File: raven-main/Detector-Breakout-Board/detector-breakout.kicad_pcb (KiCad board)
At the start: 2 copper layers, 46 parts, among them J1 DeployLipo, J3 Conn_01x04, J9 UCLipo, Q1 SQJQ100EL, U7 TPS7A4701xRGW

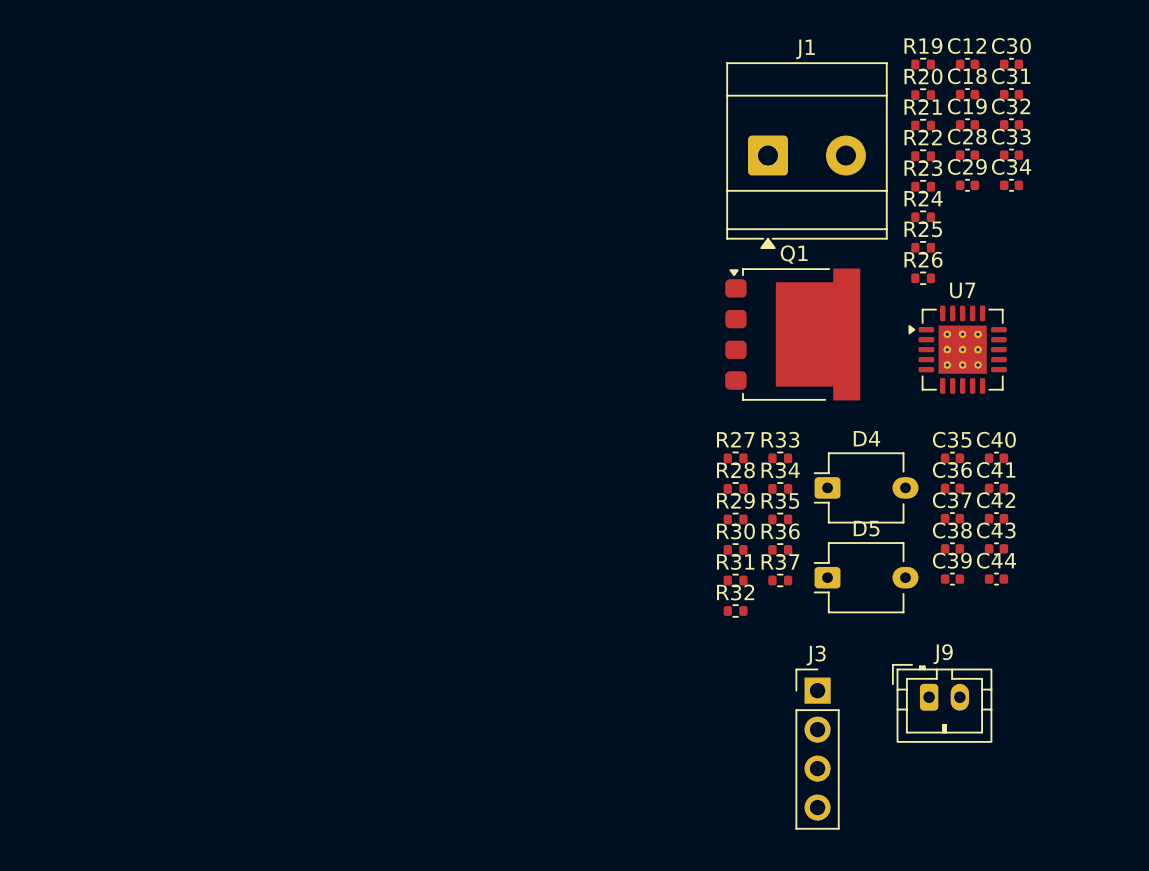
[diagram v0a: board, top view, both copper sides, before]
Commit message: Updated pcb layout
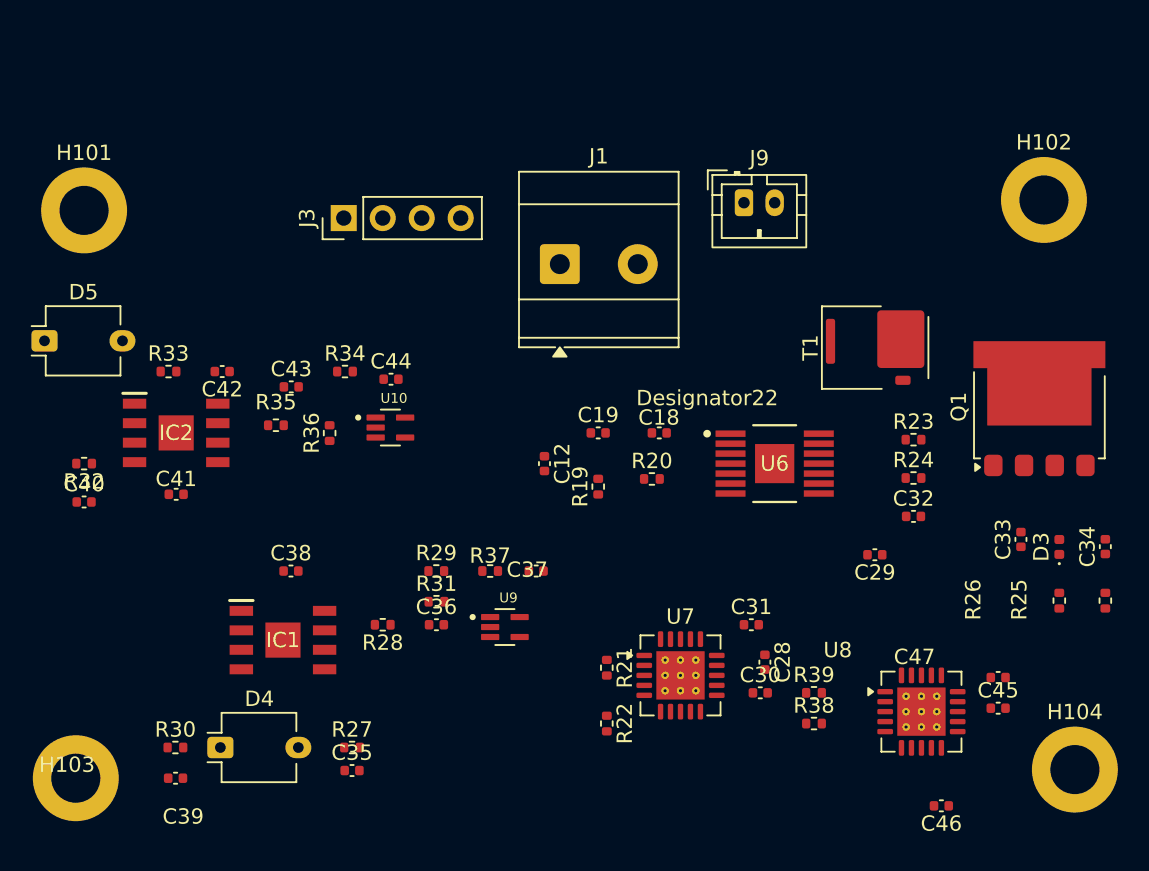
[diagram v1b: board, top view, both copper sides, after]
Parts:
- added C45: 10uF, Capacitor_SMD:C_0402_1005Metric, F.Cu at (133.1, 90.4)
- added C46: 1uF, Capacitor_SMD:C_0402_1005Metric, F.Cu at (129.4, 96.8)
- added C47: 47uF, Capacitor_SMD:C_0402_1005Metric, F.Cu at (133.1, 88.4)
- added D3: D, Diode_SMD:D_0402_1005Metric, F.Cu at (137.0, 79.9)
- added H101: MountingHole_Pad, MountingHole:MountingHole_3.2mm_M3_DIN965_Pad, F.Cu at (73.5, 58.0)
- added H102: MountingHole_Pad, MountingHole:MountingHole_3.2mm_M3_DIN965_Pad, F.Cu at (136.0, 57.3)
- added H103: MountingHole_Pad, MountingHole:MountingHole_3.2mm_M3_DIN965_Pad, F.Cu at (73.0, 95.0)
- added H104: MountingHole_Pad, MountingHole:MountingHole_3.2mm_M3_DIN965_Pad, F.Cu at (138.1, 94.4)
- added IC1: ADA4817-1ARDZ-R7, ADA4817-1ARDZ-R7:SOIC127P600X175-9N, F.Cu at (86.5, 86.0)
- added IC2: ADA4817-1ARDZ-R7, ADA4817-1ARDZ-R7:SOIC127P600X175-9N, F.Cu at (79.5, 72.5)
- added R38: 13.3k, Resistor_SMD:R_0402_1005Metric, F.Cu at (121.1, 91.4)
- added R39: 9.76k, Resistor_SMD:R_0402_1005Metric, F.Cu at (121.1, 89.4)
- added T1: Transformer_1P_1S, Transistor_Power:GaN_Systems_GaNPX-3_5x6.6mm_Drain2.93x0.6mm, F.Cu at (125.0, 66.9)
- added U10: TLV3201AIDCKT, TLV3201AIDCKT:SOT65P210X110-5N, F.Cu at (93.5, 72.2)
- added U6: LM5185QPWPRQ1, footprints:PWP0014G-IPC_A, F.Cu at (118.5, 74.5)
- added U8: TPS7A4701xRGW, Package_DFN_QFN:Texas_RGW0020A_VQFN-20-1EP_5x5mm_P0.65mm_EP3.15x3.15mm_ThermalVias, F.Cu at (128.1, 90.7)
- added U9: TLV3201AIDCKT, TLV3201AIDCKT:SOT65P210X110-5N, F.Cu at (100.9, 85.2)
- R22: value 10k -> 9.76k
- moved C40 59.5 mm to (73.5, 77.0)
- moved C41 53.5 mm to (79.5, 76.5)
- moved D5 53.3 mm to (70.9, 66.5)
- moved C39 52.3 mm to (79.5, 95.0), turned to 180 degrees
- moved C42 51.4 mm to (82.5, 68.5), turned to 180 degrees
- moved C43 47.2 mm to (87.0, 69.5)
- moved C30 44.1 mm to (117.6, 89.4)
- moved C35 44.1 mm to (91.0, 94.5)
- moved J3 43.6 mm to (90.4, 58.5), turned to 90 degrees
- moved R32 43.5 mm to (73.5, 74.5), turned to 180 degrees
- moved C38 43.1 mm to (87.0, 81.5)
- moved D4 43.0 mm to (82.4, 93.0)
- moved R22 42.3 mm to (107.6, 91.4), turned to -90 degrees
- moved C44 41.5 mm to (93.5, 69.0)
- moved R21 40.9 mm to (107.6, 87.8), turned to -90 degrees
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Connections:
- C37 pad 2: +5V -> +3V3
- C44 pad 2: +5V -> +3V3

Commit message: Began PCB layout (transformer and diode brand not confirmed)
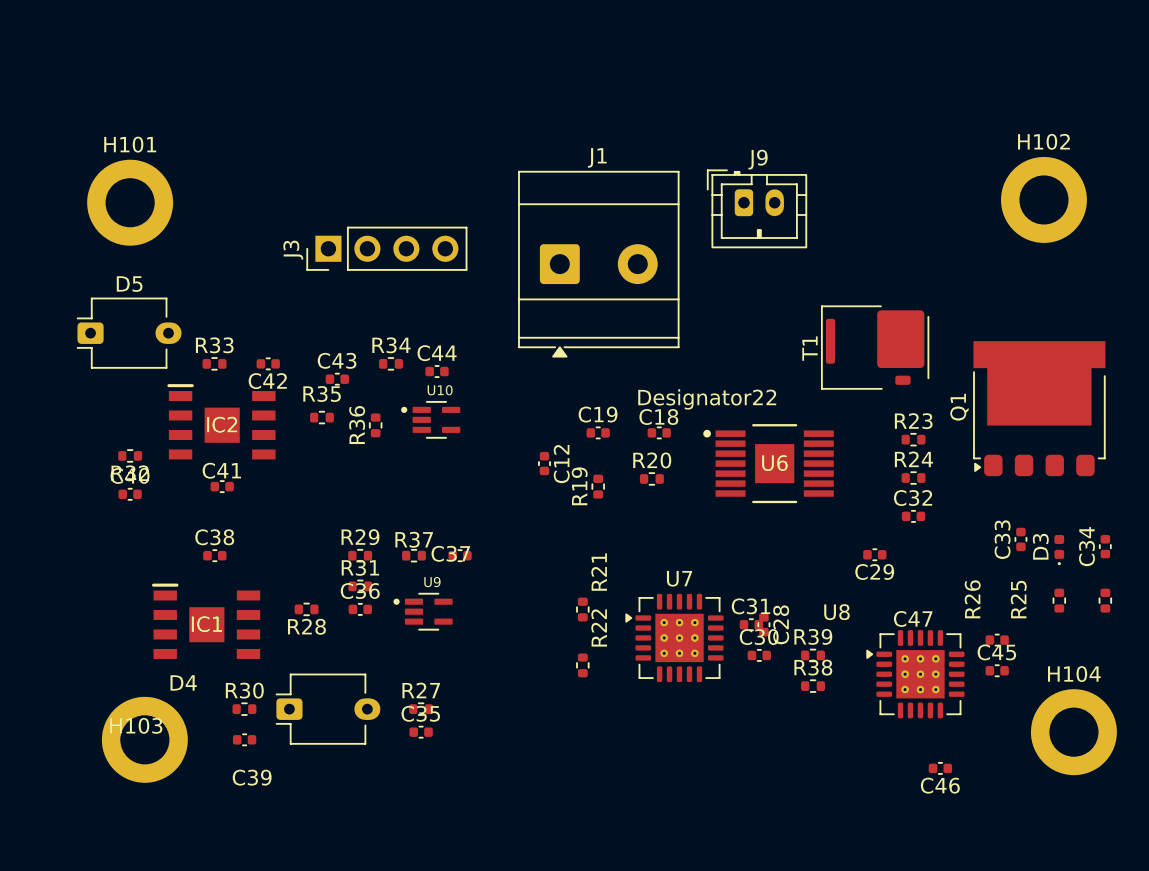
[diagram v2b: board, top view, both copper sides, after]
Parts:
- moved C35 5.15 mm to (95.5, 92.0)
- moved C39 5.15 mm to (84.0, 92.5)
- moved D4 5.15 mm to (86.9, 90.5)
- moved H103 5.15 mm to (77.5, 92.5)
- moved R27 5.15 mm to (95.5, 90.5)
- moved R30 5.15 mm to (84.0, 90.5)
- moved C38 5.06 mm to (82.0, 80.5)
- moved R29 5.06 mm to (91.5, 80.5)
- moved U9 5.06 mm to (96.0, 84.2)
- moved C36 5.06 mm to (91.5, 84.0)
- moved C37 5.06 mm to (98.0, 80.5)
- moved IC1 5.06 mm to (81.5, 85.0)
- moved R28 5.06 mm to (88.0, 84.0)
- moved R31 5.06 mm to (91.5, 82.5)
- moved R37 5.06 mm to (95.0, 80.5)
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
